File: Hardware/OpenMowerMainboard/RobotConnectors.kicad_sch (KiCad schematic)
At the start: 38 parts, among them J1 Conn_02x11_Top_Bottom, J10 Conn_01x05, J11 Conn_01x03_Male, J12 Conn_01x03_Male, J13 Conn_01x03_Male, J14 Conn_01x03_Male, J15 Conn_01x02_Male, J17 Conn_01x02, J18 Conn_01x02, J19 Conn_01x04, J2 Conn_02x04_Top_Bottom, J3 Conn_01x02, J5 Conn_01x04, J6 Conn_01x04, J7 Conn_01x04, J8 Conn_01x04, J9 Conn_01x04

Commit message: wip schematic
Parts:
- added F1, F2, F3, F4: Fuse, MyModules:Fuseholder5x20_horiz_open_inline_Type-I, symbol Device:Fuse
- gave numbers to parts that had none: 1
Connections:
- net V_BATT: now also F4.2; no longer D3.1 (K), J2.7 (Pin_7)
- net V_BATT_ALWAYS_ON: now also F1.1; no longer J2.1 (Pin_1), J2.3 (Pin_3)
- net V_CHARGE: now also F2.1; no longer J3.2 (Pin_2)
- net at D3.2 (A): now also F3.2; no longer J15.2 (Pin_2)
- new net: F2.2, J3.2 (Pin_2)
- new net: F1.2, J2.1 (Pin_1), J2.3 (Pin_3)
- new net: D3.1 (K), F4.1, J2.7 (Pin_7)
- new net: F3.1, J15.2 (Pin_2)
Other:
- moved on the sheet: J15

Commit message: added footprints to schematic
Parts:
- removed F1: Fuse, MyModules:Fuseholder5x20_horiz_open_inline_Type-I, symbol Device:Fuse
- removed R10, R15, R16, R19, R20, R3, R6, R9: R, Resistor_SMD:R_0805_2012Metric, symbol Device:R
- D2, D3: footprint (none) -> Diode_SMD:D_SMA_Handsoldering
- R1, R13, R14, R17, R18, R2, R21, R22, R7, R8: footprint Resistor_SMD:R_0805_2012Metric -> Resistor_SMD:R_0805_2012Metric_Pad1.20x1.40mm_HandSolder
- R51: footprint Resistor_SMD:R_Shunt_Vishay_WSK2512_6332Metric_T2.66mm -> Resistor_SMD:R_2512_6332Metric_Pad1.40x3.35mm_HandSolder
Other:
- added sheet LevelShifter5 (LEVEL_SHIFTER.kicad_sch)
- added sheet LevelShifter6 (LEVEL_SHIFTER.kicad_sch)
- added sheet LevelShifter7 (LEVEL_SHIFTER.kicad_sch)
- added sheet LevelShifter8 (LEVEL_SHIFTER.kicad_sch)
- moved on the sheet: J1, J11, J12, J13, J14, J17, J18, J19, J5, J6, J7, J8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

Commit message: wip
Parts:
- removed R1, R13, R14, R17, R18, R2, R21, R22, R7, R8: R, Resistor_SMD:R_0805_2012Metric_Pad1.20x1.40mm_HandSolder, symbol Device:R
- added IC1: 74ALVC164245DGG,11, SOP50P810X120-48N, symbol 74ALVC164245DGG_11:74ALVC164245DGG,11
- added JP2, JP3: SolderJumper_3_Bridged12, Jumper:SolderJumper-3_P1.3mm_Bridged12_Pad1.0x1.5mm, symbol Jumper:SolderJumper_3_Bridged12
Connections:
- net +3V3: now also IC1.31 (VCC(A)_1), IC1.42 (VCC(A)_2), JP2.3 (B), JP3.1 (A)
- net +5V: now also IC1.18 (VCC(B)_2), IC1.7 (VCC(B)_1)
- net GND: now also IC1.10 (GND_2), IC1.15 (GND_3), IC1.21 (GND_4), IC1.25 (~{2OE}), IC1.26 (2A7), IC1.27 (2A6), IC1.28 (GND_5), IC1.29 (2A5), IC1.34 (GND_6), IC1.39 (GND_7), IC1.4 (GND_1), IC1.45 (GND_8), IC1.48 (~{1OE}), JP2.1 (A), JP3.3 (B)
- net USS_1_ECHO: now also IC1.47 (1A0)
- net USS_1_ECHO_5V: now also IC1.2 (1B0)
- net USS_1_TRIGGER: now also IC1.30 (2A4)
- net USS_1_TRIGGER_5V: now also IC1.19 (2B4)
- net USS_2_ECHO: now also IC1.46 (1A1)
- net USS_2_ECHO_5V: now also IC1.3 (1B1)
- net USS_2_TRIGGER: now also IC1.32 (2A3)
- net USS_2_TRIGGER_5V: now also IC1.17 (2B3)
- net USS_3_ECHO: now also IC1.44 (1A2)
- net USS_3_ECHO_5V: now also IC1.5 (1B2)
- net USS_3_TRIGGER: now also IC1.33 (2A2)
- net USS_3_TRIGGER_5V: now also IC1.16 (2B2)
- net USS_4_ECHO: now also IC1.43 (1A3)
- net USS_4_ECHO_5V: now also IC1.6 (1B3)
- net USS_4_TRIGGER: now also IC1.35 (2A1)
- net USS_4_TRIGGER_5V: now also IC1.14 (2B1)
- net USS_5_ECHO: now also IC1.41 (1A4)
- net USS_5_ECHO_5V: now also IC1.8 (1B4)
- net USS_5_TRIGGER: now also IC1.36 (2A0)
- net USS_5_TRIGGER_5V: now also IC1.13 (2B0)
- new net: IC1.1 (1DIR), JP2.2 (C)
- new net: IC1.24 (2DIR), JP3.2 (C)
- no-connect marks 2 -> 5
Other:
- removed sheet LevelShifter
- removed sheet LevelShifter1
- removed sheet LevelShifter2
- removed sheet LevelShifter3
- removed sheet LevelShifter4
- note added: "--> B to A"
- note added: "<-- A to B"
- note added: "B = 5V A = 3.3V"

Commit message: wip pcb layout
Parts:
- removed D3: D_Schottky, Diode_SMD:D_SMA_Handsoldering, symbol Device:D_Schottky
- removed F3: Fuse, MyModules:Fuseholder5x20_horiz_open_inline_Type-I, symbol Device:Fuse
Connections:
- net at F2.2, J3.2 (Pin_2): now also J15.2 (Pin_2)
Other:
- moved on the sheet: J15

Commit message: routing mostly done
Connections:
- net CHARGE_SHUNT+ renamed CHARGE_SHUNT_PLUS
- net CHARGE_SHUNT- renamed CHARGE_SHUNT_MINUS
- net SPEAKER+ renamed SPEAKER_PLUS
- net SPEAKER- renamed SPEAKER_MINUS
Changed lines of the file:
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@@
     (effects (font (size 1.27 1.27)) (justify right))
   )
-  (hierarchical_label "SPEAKER-" (shape input) (at 70.485 53.975 180)
+  (hierarchical_label "SPEAKER_MINUS" (shape input) (at 70.485 53.975 180)
     (effects (font (size 1.27 1.27)) (justify right))
   )
@@
     (effects (font (size 1.27 1.27)) (justify left))
   )
-  (hierarchical_label "CHARGE_SHUNT-" (shape output) (at 124.46 20.32 90)
+  (hierarchical_label "CHARGE_SHUNT_MINUS" (shape output) (at 124.46 20.32 90)
     (effects (font (size 1.27 1.27)) (justify left))
   )
@@
     (effects (font (size 1.27 1.27)) (justify left))
   )
-  (hierarchical_label "CHARGE_SHUNT+" (shape output) (at 114.935 20.32 90)
+  (hierarchical_label "CHARGE_SHUNT_PLUS" (shape output) (at 114.935 20.32 90)
     (effects (font (size 1.27 1.27)) (justify left))
   )
@@
     (effects (font (size 1.27 1.27)) (justify left))
   )
-  (hierarchical_label "SPEAKER+" (shape input) (at 70.485 51.435 180)
+  (hierarchical_label "SPEAKER_PLUS" (shape input) (at 70.485 51.435 180)
     (effects (font (size 1.27 1.27)) (justify right))
   )

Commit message: WIP hardware revision
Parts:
- added D15, D16, D17, D3: D_Schottky, Diode_SMD:D_SMA_Handsoldering, symbol Device:D_Schottky
- added J4: Conn_01x05, Connector_JST:JST_XH_B5B-XH-A_1x05_P2.50mm_Vertical, symbol Connector_Generic:Conn_01x05
- IC1: footprint SOP50P810X120-48N -> 74ALVC164245DGG:SOP50P810X120-48N
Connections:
- net CHARGE_SHUNT_MINUS: no longer J2.5 (Pin_5)
- net GND: now also IC1.11 (1B6), IC1.12 (1B7), IC1.9 (1B5), J4.1 (Pin_1)
- net MC_H1: now also J4.2 (Pin_2)
- net MC_H2: now also J4.3 (Pin_3)
- net MC_H3: now also J4.4 (Pin_4)
- net MC_HALL+: now also J4.5 (Pin_5)
- net V_BATT: now also D2.2 (A), D15.1 (K), D16.1 (K), D17.1 (K), D3.1 (K); no longer F4.2
- net V_CHARGE: now also D3.2 (A); no longer D2.2 (A)
- net at F2.2, J3.2 (Pin_2): no longer J15.2 (Pin_2)
- new net: D17.2 (A), J15.2 (Pin_2)
- new net MosfetSwitch/VOUT: J2.5 (Pin_5)
- new net V_BATTERY: D15.2 (A), D16.2 (A), F4.2
- no-connect marks 5 -> 8
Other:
- added sheet MosfetSwitch (mosfet_switch.kicad_sch)
- note added: "1 = P+ (Battery Voltage Always On)"
- note added: "2 = Battery GND"
- note added: "3 = Gets switched to 7 externally"
- note added: "4 = Yellow Battery Cable (for temperature measurement)"
- note added: "5 = C+ Battery Charging Voltage. (Switched externally)"
- note added: "6 = Not Connected"
- note added: "7 = Switched P+"
- note added: "8 = Green Battery Cable (for temperature measurement)"
- note removed: "Gelb zum Akku"
- note removed: "Grün zum Akku"
- note removed: "TODO: Stecker einfügen"
- moved on the sheet: D2, F2, F4, J15, J17, J18, J3, R51

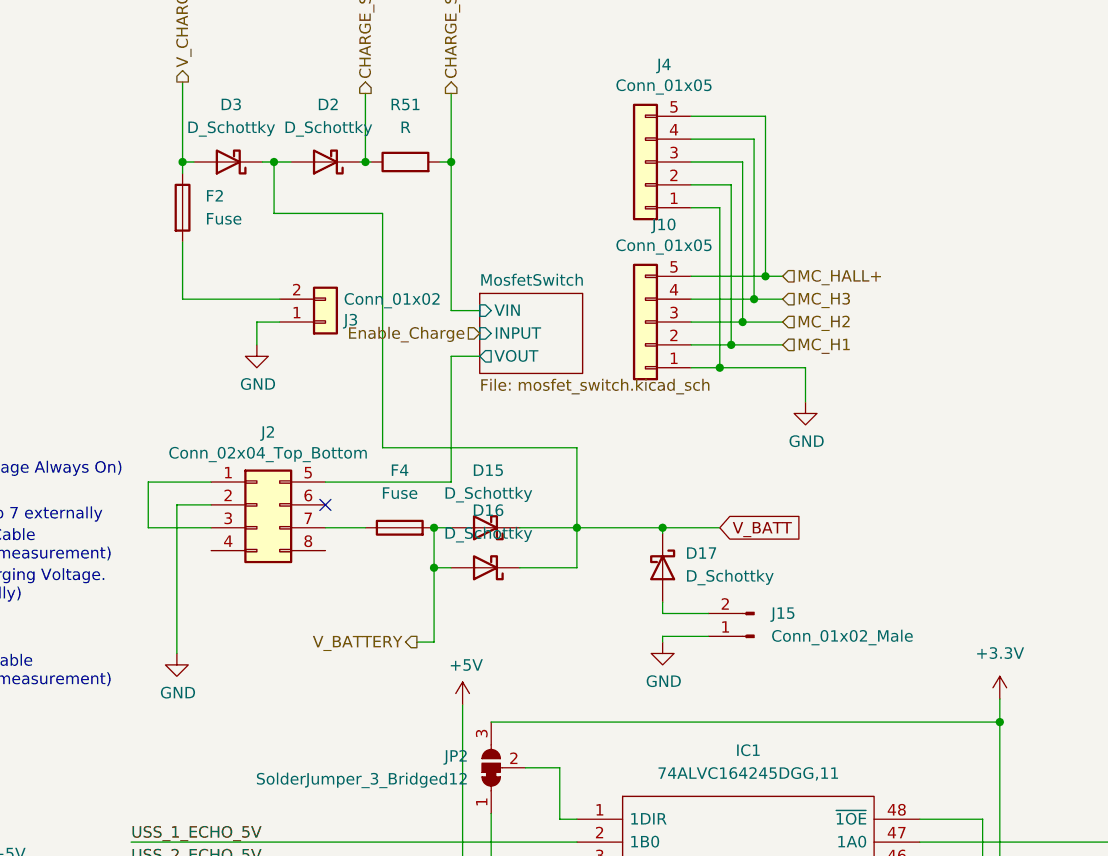
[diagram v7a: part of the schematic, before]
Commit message: v0_9_1 mainboard rework
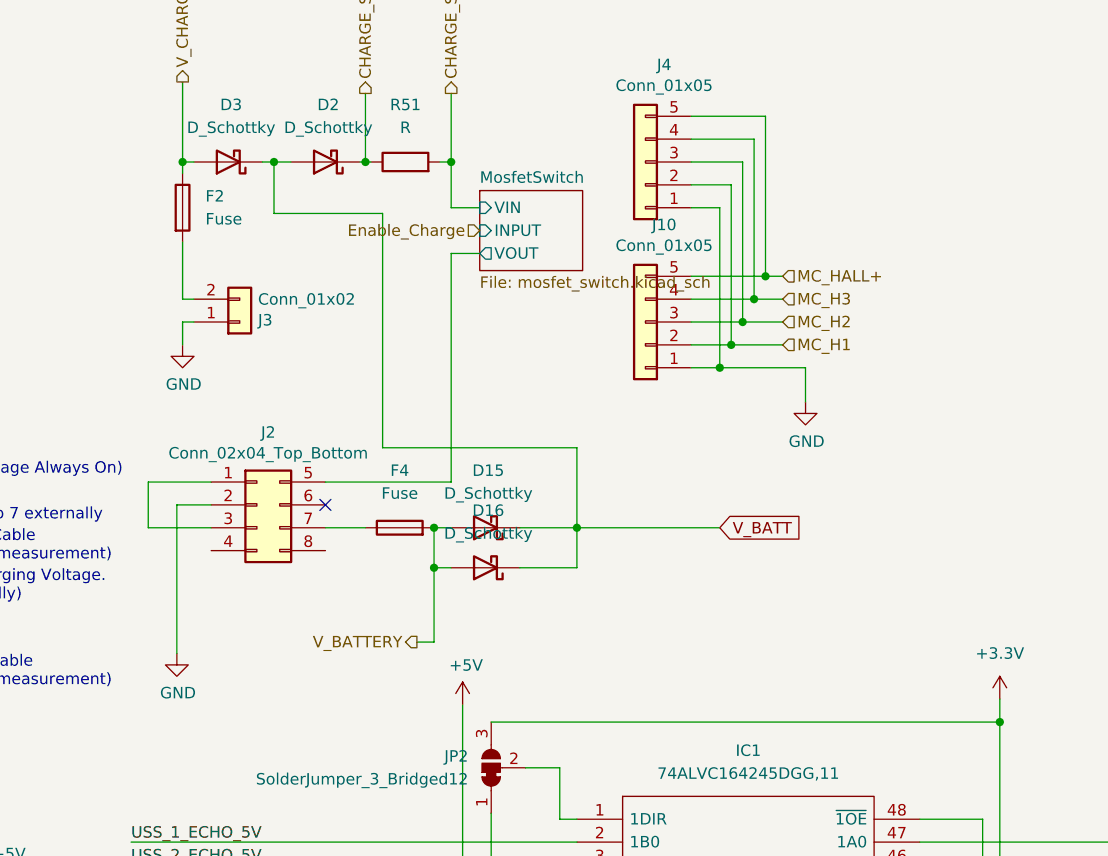
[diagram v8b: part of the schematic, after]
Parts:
- removed D17: D_Schottky, Diode_SMD:D_SMA_Handsoldering, symbol Device:D_Schottky
- removed J15: Conn_01x02_Male, Connector_AMASS:AMASS_XT60-M_1x02_P7.20mm_Vertical, symbol Connector:Conn_01x02_Male
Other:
- moved on the sheet: J3
